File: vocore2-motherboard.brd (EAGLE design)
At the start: 100 x 100 mm, 93 parts, among them IC1 AP63205, IC2 FE1.1S, IC3 LM3671MF-3.3, IC4 LM3671MF-3.3, IC5 LM3671MF-3.3, IC6 FT232R, IC7 742G17DBV, J1 RJHSE-5381, J2 TE_1775470-8, J3 AMPHENOL_1140084168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

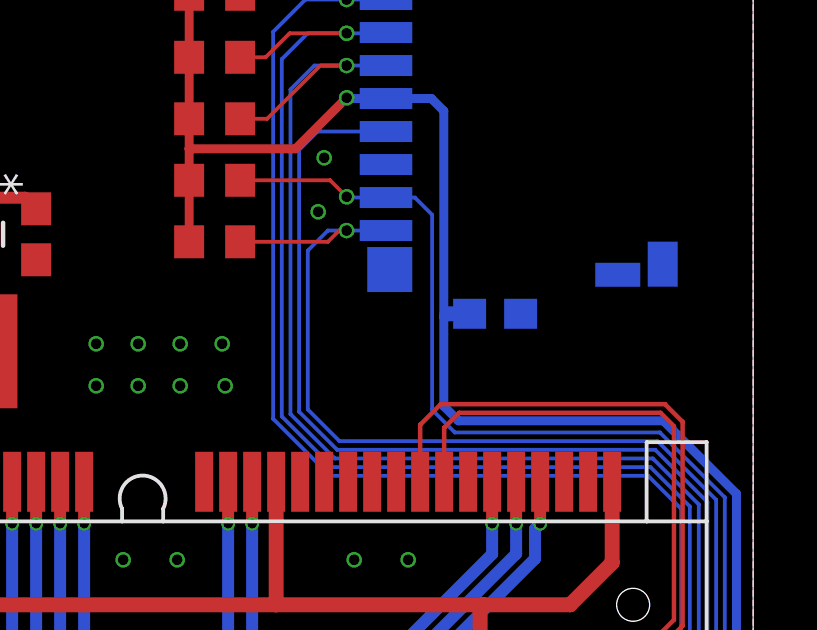
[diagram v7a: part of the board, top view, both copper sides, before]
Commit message: fix: switched SD_D0 and SD_D1
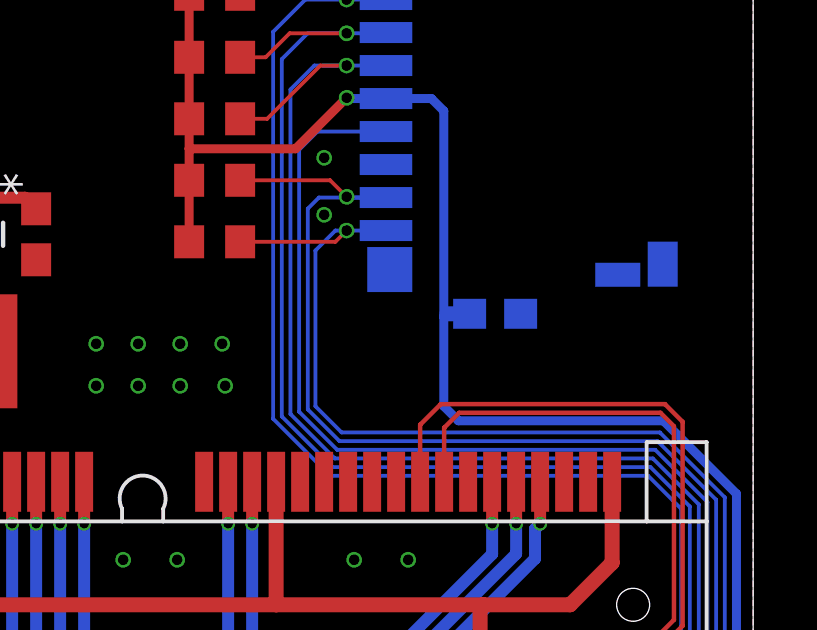
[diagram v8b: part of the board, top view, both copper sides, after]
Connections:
- net VC_SD_D0: now also J3.7, R11.1; no longer J3.8, R19.1
- net VC_SD_D1: now also J3.8, R19.1; no longer J3.7, R11.1
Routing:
- net VC_SD_D0: track 102.9 -> 105.6 mm
- net VC_SD_D1: track 102.5 -> 104.6 mm
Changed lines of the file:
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@@
 <via x="32.4" y="55.3" extent="1-16" drill="0.35"/>
 <via x="35.7" y="62.9" extent="1-16" drill="0.35"/>
-<via x="35.5" y="61.1" extent="1-16" drill="0.35"/>
+<via x="35.7" y="61" extent="1-16" drill="0.35"/>
 <via x="-5.8" y="4.1" extent="1-16" drill="0.35"/>
 <via x="-5.8" y="2.9" extent="1-16" drill="0.35"/>
@@
 <contactref element="U1" pad="51_2"/>
 <wire x1="17.762" y1="5.84" x2="17.762" y2="7.192" width="1.12" layer="1"/>
-<contactref element="J3" pad="7"/>
 <wire x1="40.59125" y1="4.2555" x2="44.29125" y2="7.9555" width="0.127" layer="16"/>
 <wire x1="44.29125" y1="7.9555" x2="47.59225" y2="7.9555" width="0.127" layer="16"/>
@@
 <wire x1="19.4647" y1="5.4893" x2="22.86525" y2="5.4893" width="0.127" layer="16"/>
 <wire x1="22.86525" y1="5.4893" x2="24.09905" y2="4.2555" width="0.127" layer="16"/>
-<wire x1="40.0555" y1="53.7445" x2="39.3" y2="54.5" width="0.127" layer="16"/>
 <wire x1="49.0556" y1="51.58015" x2="46.89125" y2="53.7445" width="0.127" layer="16"/>
-<wire x1="46.89125" y1="53.7445" x2="40.0555" y2="53.7445" width="0.127" layer="16"/>
-<wire x1="39.3" y1="61" x2="39.3" y2="54.5" width="0.127" layer="16"/>
+<wire x1="46.89125" y1="53.7445" x2="36.2833125" y2="53.7445" width="0.127" layer="16"/>
 <wire x1="49.0556" y1="9.41885" x2="49.0556" y2="51.58015" width="0.127" layer="16"/>
-<wire x1="37.762" y1="61.575" x2="38.725" y2="61.575" width="0.127" layer="16"/>
-<wire x1="38.725" y1="61.575" x2="39.3" y2="61" width="0.127" layer="16"/>
-<contactref element="R11" pad="1"/>
-<wire x1="32.9" y1="62.15" x2="35.9" y2="62.15" width="0.127" layer="1"/>
-<wire x1="35.9" y1="62.15" x2="36.45" y2="61.6" width="0.127" layer="1"/>
-<via x="36.45" y="61.6" extent="1-16" drill="0.35"/>
-<wire x1="36.45" y1="61.6" x2="36.475" y2="61.575" width="0.127" layer="16"/>
-<wire x1="36.475" y1="61.575" x2="37.762" y2="61.575" width="0.127" layer="16"/>
+<contactref element="J3" pad="8"/>
+<contactref element="R19" pad="1"/>
+<wire x1="36.2833125" y1="53.7445" x2="35.4096" y2="54.6182125" width="0.127" layer="16"/>
+<wire x1="35.4096" y1="59.8096" x2="35.4096" y2="54.6182125" width="0.127" layer="16"/>
+<wire x1="37.762" y1="60.475" x2="36.45" y2="60.475" width="0.127" layer="16"/>
+<wire x1="36.45" y1="60.475" x2="36.075" y2="60.475" width="0.127" layer="16"/>
+<wire x1="36.075" y1="60.475" x2="35.4096" y2="59.8096" width="0.127" layer="16"/>
+<wire x1="32.9" y1="60.1" x2="36.075" y2="60.1" width="0.127" layer="1"/>
+<wire x1="36.075" y1="60.1" x2="36.45" y2="60.475" width="0.127" layer="1"/>
+<via x="36.45" y="60.475" extent="1-16" drill="0.35"/>
 </signal>
 <signal name="VC_SD_D2">
@@
 <contactref element="U1" pad="52_1"/>
 <wire x1="19.032" y1="5.84" x2="19.032" y2="7.192" width="1.12" layer="1"/>
-<contactref element="J3" pad="8"/>
 <wire x1="24.1773" y1="4.5444" x2="40.513" y2="4.5444" width="0.127" layer="16"/>
 <wire x1="40.513" y1="4.5444" x2="44.213" y2="8.2444" width="0.127" layer="16"/>
@@
 <wire x1="36.213" y1="53.4556" x2="35.1556" y2="54.513" width="0.127" layer="16"/>
 <wire x1="48.7667" y1="9.6471" x2="48.7667" y2="51.5019" width="0.127" layer="16"/>
-<wire x1="35.1556" y1="59.8056" x2="35.1556" y2="54.513" width="0.127" layer="16"/>
-<wire x1="37.762" y1="60.475" x2="36.45" y2="60.475" width="0.127" layer="16"/>
-<wire x1="36.45" y1="60.475" x2="35.825" y2="60.475" width="0.127" layer="16"/>
-<wire x1="35.825" y1="60.475" x2="35.1556" y2="59.8056" width="0.127" layer="16"/>
-<contactref element="R19" pad="1"/>
-<wire x1="32.9" y1="60.1" x2="35.825" y2="60.1" width="0.127" layer="1"/>
-<wire x1="36.2" y1="60.475" x2="36.45" y2="60.475" width="0.127" layer="1"/>
-<wire x1="36.2" y1="60.475" x2="35.825" y2="60.1" width="0.127" layer="1"/>
-<via x="36.45" y="60.475" extent="1-16" drill="0.35"/>
+<contactref element="J3" pad="7"/>
+<contactref element="R11" pad="1"/>
+<wire x1="32.9" y1="62.15" x2="35.9" y2="62.15" width="0.127" layer="1"/>
+<wire x1="35.9" y1="62.15" x2="36.45" y2="61.6" width="0.127" layer="1"/>
+<via x="36.45" y="61.6" extent="1-16" drill="0.35"/>
+<wire x1="36.45" y1="61.6" x2="36.475" y2="61.575" width="0.127" layer="16"/>
+<wire x1="36.475" y1="61.575" x2="37.762" y2="61.575" width="0.127" layer="16"/>
+<wire x1="37.762" y1="61.575" x2="35.525" y2="61.575" width="0.127" layer="16"/>
+<wire x1="35.1556" y1="54.513" x2="35.1556" y2="61.2056" width="0.127" layer="16"/>
+<wire x1="35.525" y1="61.575" x2="35.1556" y2="61.2056" width="0.127" layer="16"/>
 </signal>
 <signal name="X3_P3">
